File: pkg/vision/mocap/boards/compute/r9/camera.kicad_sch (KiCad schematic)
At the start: 5 parts, among them J1 FH34SRJ-22S-0.5SH_50_, J2 CAM_EXT_TRIG, J3 CAM_STROBE

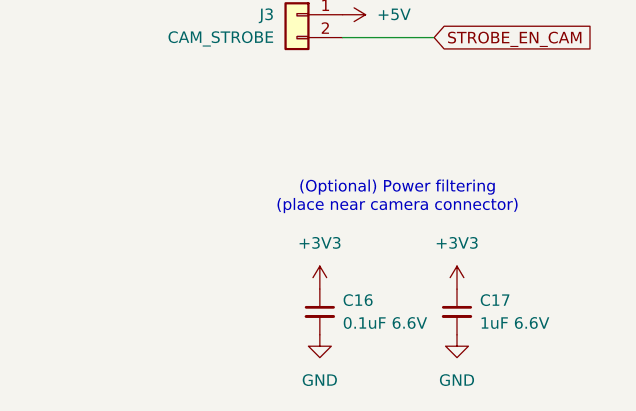
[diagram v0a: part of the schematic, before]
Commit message: New mocap compute board revisions.
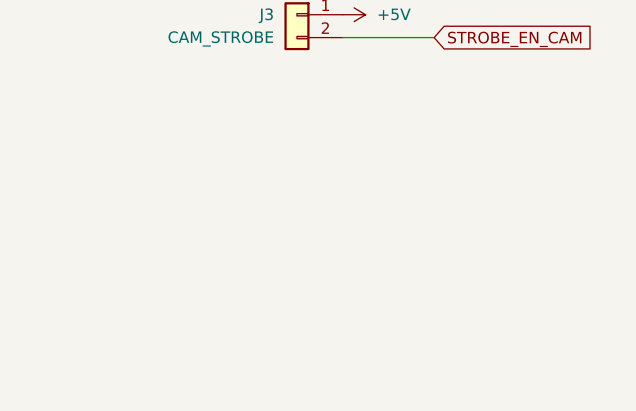
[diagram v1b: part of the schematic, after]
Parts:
- removed C16: 0.1uF 6.6V, Capacitor_SMD:C_0603_1608Metric, symbol Device:C_Small
- removed C17: 1uF 6.6V, Capacitor_SMD:C_0603_1608Metric, symbol Device:C_Small
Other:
- note removed: "(Optional) Power filtering (place near camera connector)"
